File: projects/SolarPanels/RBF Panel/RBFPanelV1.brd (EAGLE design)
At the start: 99.5 x 82.5 mm, 43 parts

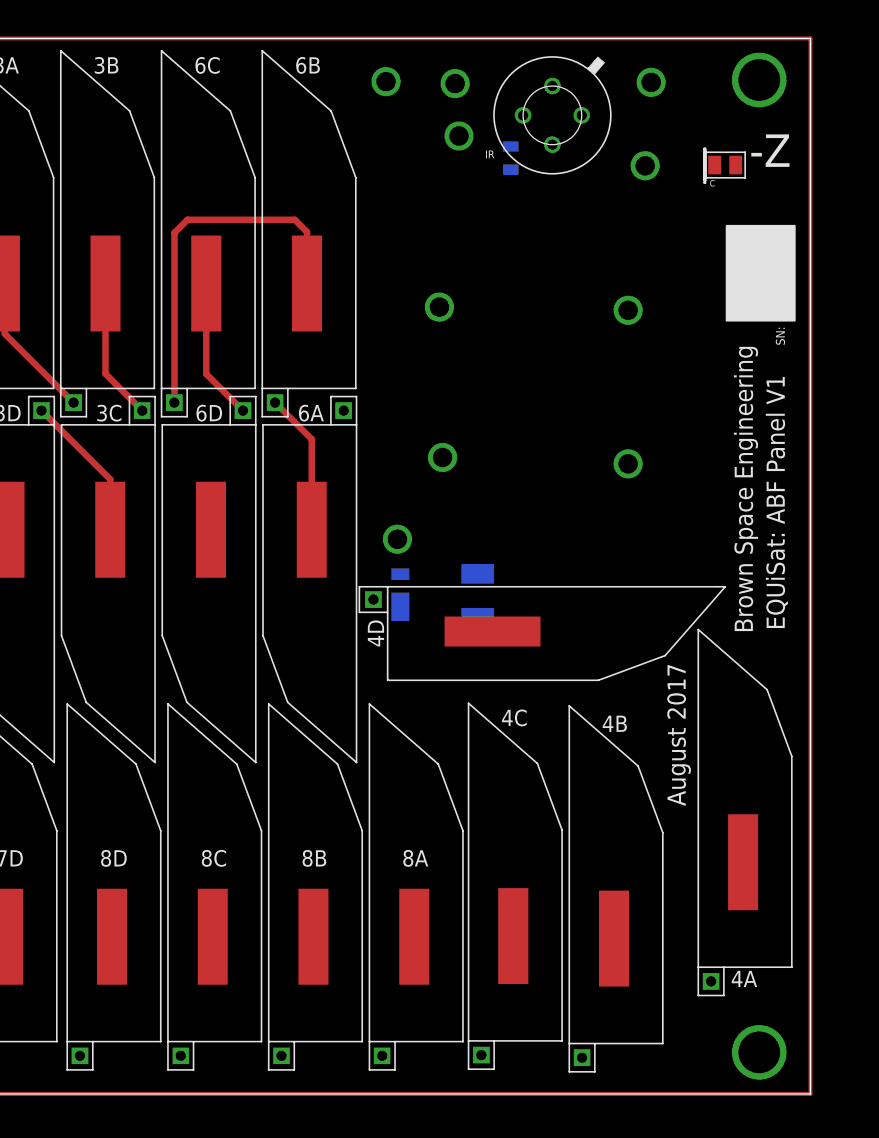
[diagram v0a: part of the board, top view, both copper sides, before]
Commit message: Added RBF switches to library. (changed ABF to RBF) Added RBF switches and routing to RBF Panel. Vectorized all text on solar panel boards and rearranged as needed.
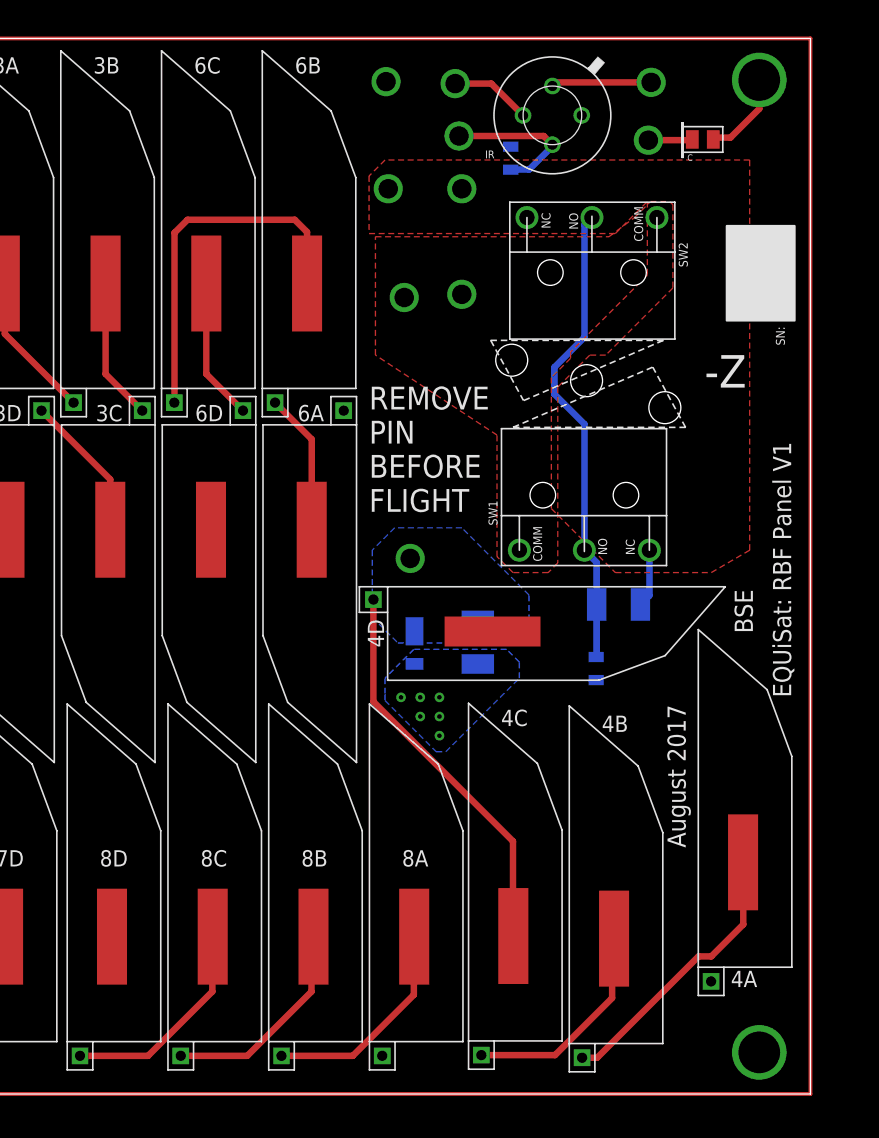
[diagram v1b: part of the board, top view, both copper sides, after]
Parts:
- added R2: 10M, BrownSpaceEngineering:0805
- added R3: 0R, BrownSpaceEngineering:1210
- added SW1, SW2: D2F-L-A, BrownSpaceEngineering:D2F-L-A
- moved V4 25.1 mm to (72.2, 70.8), turned to 270 degrees
- moved V3 21.0 mm to (66.5, 70.8), turned to 270 degrees
- moved V1 12.9 mm to (67.8, 62.2), turned to 270 degrees
- moved D1 4.26 mm to (68.6, 35.1), turned to 270 degrees
- moved R1 3.62 mm to (73.5, 35.3), turned to 90 degrees
- moved PD 2.66 mm to (91.1, 74.2)
- moved PD-OUT 2.02 mm to (86.8, 74.5)
- moved V2 2.02 mm to (72.2, 62.5), turned to 270 degrees
- moved PWR-OUT 1.80 mm to (68.2, 41.9)
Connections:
- new net N$13: R2.1, R3.P$1, SW1.P$2, SW2.P$2
- net GND: now also R2.2
- net LION-IN: now also SW1.P$1, SW2.P$1
- net LION-OUT: now also R3.P$2, SW1.P$3, SW2.P$3
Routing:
- net N$13: track 0.00 -> 37.0 mm
- net N$10: track 0.00 -> 30.8 mm
- net N$12: track 0.00 -> 21.8 mm
- net N$25: track 0.00 -> 16.9 mm
- net N$11: track 0.00 -> 16.8 mm
- net N$23: track 0.00 -> 16.7 mm
- net N$24: track 0.00 -> 16.7 mm
- net 3V3: track 0.00 -> 11.7 mm
- net SCL: track 0.00 -> 7.84 mm
- net GND: track 0.00 -> 6.84 mm
- net SDA: track 0.00 -> 6.34 mm
- net LION-OUT: track 0.00 -> 4.54 mm
- net PD-OUT: track 0.00 -> 3.46 mm
- added copper zone on layer 1, net LION-IN
- added copper zone on layer 1, net LION-OUT
- added copper zone on layer 16, net SP-PWR
- added copper zone on layer 16, net SP-PWR-OUT
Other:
- board text added: "BSE"
- board text added: "EQUiSat: RBF Panel V1"
- board text added: "REMOVE PIN BEFORE FLIGHT"
- board text removed: "Brown Space Engineering"
- board text removed: "EQUiSat: ABF Panel V1"
